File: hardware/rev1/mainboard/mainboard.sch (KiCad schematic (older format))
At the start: 59 parts, among them J1 CONN_05X2SHD, J2 Conn_01x10_Female, J3 Conn_01x10_Female, U1 LM1117-5.0, U2 LM1117-3.3, U3 SAMD51J, U4 OPA197, U5 W25Q32FVSS, U6 AD5685xRUZ, U7 SN74AHCT125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

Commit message: Switch 3v3 regulator to TPS796
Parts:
- removed U2: LM1117-3.3, Package_TO_SOT_SMD:SOT-223-3_TabPin2, symbol Regulator_Linear:LM1117-3.3
- added C21: 1uF, Capacitor_SMD:C_1206_3216Metric_Pad1.42x1.75mm_HandSolder, symbol Device:C
- added U2: TPS79633, Package_TO_SOT_SMD:SOT-223-6_TabPin3, symbol mainboard-rescue:TPS79633
- C7: value 22uF -> 4.7uF
- C8: value 22uF -> 0.1uF
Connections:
- wire segments 57 -> 61
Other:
- moved on the sheet: TP2
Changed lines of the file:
@@
 $EndComp
-$Comp
-L Regulator_Linear:LM1117-3.3 U2
-U 1 1 5D1ED054
-P 1400 2950
-F 0 "U2" H 1400 3192 50  0000 C CNN
-F 1 "LM1117-3.3" H 1400 3101 50  0000 C CNN
-F 2 "Package_TO_SOT_SMD:SOT-223-3_TabPin2" H 1400 2950 50  0001 C CNN
-F 3 "http://www.ti.com/lit/ds/symlink/lm1117.pdf" H 1400 2950 50  0001 C CNN
-	1    1400 2950
-	1    0    0    -1
-$EndComp
-$Comp
-L Device:C C7
-U 1 1 5D1EE7D9
-P 850 3100
-F 0 "C7" H 965 3146 50  0000 L CNN
-F 1 "22uF" H 965 3055 50  0000 L CNN
-F 2 "Capacitor_SMD:C_1206_3216Metric_Pad1.42x1.75mm_HandSolder" H 888 2950 50  0001 C CNN
-F 3 "~" H 850 3100 50  0001 C CNN
-	1    850  3100
-	1    0    0    -1
-$EndComp
-$Comp
-L Device:C C8
-U 1 1 5D341659
-P 1900 3100
-F 0 "C8" H 2015 3146 50  0000 L CNN
-F 1 "22uF" H 2015 3055 50  0000 L CNN
-F 2 "Capacitor_SMD:C_1206_3216Metric_Pad1.42x1.75mm_HandSolder" H 1938 2950 50  0001 C CNN
-F 3 "~" H 1900 3100 50  0001 C CNN
-	1    1900 3100
-	1    0    0    -1
-$EndComp
-Wire Wire Line
-	850  2950 1100 2950
-Wire Wire Line
-	1700 2950 1900 2950
-$Comp
-L power:GND #PWR0109
-U 1 1 5D1EFC36
-P 850 3250
-F 0 "#PWR0109" H 850 3000 50  0001 C CNN
-F 1 "GND" V 855 3122 50  0000 R CNN
-F 2 "" H 850 3250 50  0001 C CNN
-F 3 "" H 850 3250 50  0001 C CNN
-	1    850  3250
-	1    0    0    -1
-$EndComp
-$Comp
-L power:GND #PWR0110
-U 1 1 5D1F0162
-P 1400 3250
-F 0 "#PWR0110" H 1400 3000 50  0001 C CNN
-F 1 "GND" V 1405 3122 50  0000 R CNN
-F 2 "" H 1400 3250 50  0001 C CNN
-F 3 "" H 1400 3250 50  0001 C CNN
-	1    1400 3250
-	1    0    0    -1
-$EndComp
-$Comp
-L power:GND #PWR0111
-U 1 1 5D34165C
-P 1900 3250
-F 0 "#PWR0111" H 1900 3000 50  0001 C CNN
-F 1 "GND" V 1905 3122 50  0000 R CNN
-F 2 "" H 1900 3250 50  0001 C CNN
-F 3 "" H 1900 3250 50  0001 C CNN
-	1    1900 3250
-	1    0    0    -1
-$EndComp
-$Comp
-L power:+12V #PWR0112
-U 1 1 5D1F0712
-P 850 2950
-F 0 "#PWR0112" H 850 2800 50  0001 C CNN
-F 1 "+12V" H 865 3123 50  0000 C CNN
-F 2 "" H 850 2950 50  0001 C CNN
-F 3 "" H 850 2950 50  0001 C CNN
-	1    850  2950
-	1    0    0    -1
-$EndComp
-Connection ~ 850  2950
-$Comp
-L power:+3V3 #PWR0113
-U 1 1 5D1F0A40
-P 1900 2950
-F 0 "#PWR0113" H 1900 2800 50  0001 C CNN
-F 1 "+3V3" V 1900 3150 50  0000 C CNN
-F 2 "" H 1900 2950 50  0001 C CNN
-F 3 "" H 1900 2950 50  0001 C CNN
-	1    1900 2950
-	0    1    1    0
-$EndComp
-Connection ~ 1900 2950
 $Comp
 L Device:C C1
@@
 L Connector:TestPoint TP2
 U 1 1 5D263C38
-P 1900 2950
-F 0 "TP2" H 1950 3200 50  0000 L CNN
-F 1 "3.3v" H 1800 3200 50  0000 L CNN
-F 2 "TestPoint:TestPoint_THTPad_D1.5mm_Drill0.7mm" H 2100 2950 50  0001 C CNN
-F 3 "~" H 2100 2950 50  0001 C CNN
-	1    1900 2950
+P 2075 2850
+F 0 "TP2" H 2125 3100 50  0000 L CNN
+F 1 "3.3v" H 1975 3100 50  0000 L CNN
+F 2 "TestPoint:TestPoint_THTPad_D1.5mm_Drill0.7mm" H 2275 2850 50  0001 C CNN
+F 3 "~" H 2275 2850 50  0001 C CNN
+	1    2075 2850
 	1    0    0    -1
 $EndComp
@@
 	1    0    0    -1
 $EndComp
+$Comp
+L mainboard-rescue:TPS79633 U2
+U 1 1 5E1C19BB
+P 1475 2950
+F 0 "U2" H 1475 3292 50  0000 C CNN
+F 1 "TPS79633" H 1475 3201 50  0000 C CNN
+F 2 "Package_TO_SOT_SMD:SOT-223-6_TabPin3" H 1475 3275 50  0001 C CIN
+F 3 "http://www.ti.com/lit/ds/symlink/tps79333-ep.pdf" H 1475 3000 50  0001 C CNN
+	1    1475 2950
+	1    0    0    -1
+$EndComp
+Wire Wire Line
+	1175 3000 1000 3000
+Wire Wire Line
+	1000 3000 1000 2850
+Wire Wire Line
+	1175 2850 1000 2850
+$Comp
+L power:+5V #PWR0109
+U 1 1 5E1C6497
+P 800 2850
+F 0 "#PWR0109" H 800 2700 50  0001 C CNN
+F 1 "+5V" V 815 2978 50  0000 L CNN
+F 2 "" H 800 2850 50  0001 C CNN
+F 3 "" H 800 2850 50  0001 C CNN
+	1    800  2850
+	0    -1   -1   0
+$EndComp
+$Comp
+L Device:C C7
+U 1 1 5E1C8B98
+P 800 3000
+F 0 "C7" H 875 3075 50  0000 L CNN
+F 1 "4.7uF" H 850 2900 50  0000 L CNN
+F 2 "Capacitor_SMD:C_1206_3216Metric_Pad1.42x1.75mm_HandSolder" H 838 2850 50  0001 C CNN
+F 3 "~" H 800 3000 50  0001 C CNN
+	1    800  3000
+	1    0    0    -1
+$EndComp
+Wire Wire Line
+	775  2850 800  2850
+Connection ~ 800  2850
+Wire Wire Line
+	1000 2850 800  2850
+Connection ~ 1000 2850
+$Comp
+L power:GND #PWR0110
+U 1 1 5E1CC899
+P 1475 3250
+F 0 "#PWR0110" H 1475 3000 50  0001 C CNN
+F 1 "GND" V 1480 3122 50  0000 R CNN
+F 2 "" H 1475 3250 50  0001 C CNN
+F 3 "" H 1475 3250 50  0001 C CNN
+	1    1475 3250
+	1    0    0    -1
+$EndComp
+$Comp
+L power:+3V3 #PWR0111
+U 1 1 5E1CD045
+P 2075 2850
+F 0 "#PWR0111" H 2075 2700 50  0001 C CNN
+F 1 "+3V3" V 2075 3050 50  0000 C CNN
+F 2 "" H 2075 2850 50  0001 C CNN
+F 3 "" H 2075 2850 50  0001 C CNN
+	1    2075 2850
+	0    1    1    0
+$EndComp
+$Comp
+L Device:C C21
+U 1 1 5E1CD8BD
+P 2075 3000
+F 0 "C21" H 2190 3046 50  0000 L CNN
+F 1 "1uF" H 2190 2955 50  0000 L CNN
+F 2 "Capacitor_SMD:C_1206_3216Metric_Pad1.42x1.75mm_HandSolder" H 2113 2850 50  0001 C CNN
+F 3 "~" H 2075 3000 50  0001 C CNN
+	1    2075 3000
+	1    0    0    -1
+$EndComp
+Wire Wire Line
+	2075 2850 1775 2850
+Connection ~ 2075 2850
+$Comp
+L Device:C C8
+U 1 1 5E1D0271
+P 1775 3150
+F 0 "C8" H 1825 3250 50  0000 L CNN
+F 1 "0.1uF" H 1800 3050 50  0000 L CNN
+F 2 "Capacitor_SMD:C_1206_3216Metric_Pad1.42x1.75mm_HandSolder" H 1813 3000 50  0001 C CNN
+F 3 "~" H 1775 3150 50  0001 C CNN
+	1    1775 3150
+	1    0    0    -1
+$EndComp
+$Comp
+L power:GND #PWR0112
+U 1 1 5E1D081B
+P 1775 3300
+F 0 "#PWR0112" H 1775 3050 50  0001 C CNN
+F 1 "GND" V 1780 3172 50  0000 R CNN
+F 2 "" H 1775 3300 50  0001 C CNN
+F 3 "" H 1775 3300 50  0001 C CNN
+	1    1775 3300
+	1    0    0    -1
+$EndComp
+$Comp
+L power:GND #PWR0113
+U 1 1 5E1D0BB4
+P 2075 3150
+F 0 "#PWR0113" H 2075 2900 50  0001 C CNN
+F 1 "GND" V 2080 3022 50  0000 R CNN
+F 2 "" H 2075 3150 50  0001 C CNN
+F 3 "" H 2075 3150 50  0001 C CNN
+	1    2075 3150
+	1    0    0    -1
+$EndComp
+$Comp
+L power:GND #PWR0141
+U 1 1 5E1D0E81
+P 800 3150
+F 0 "#PWR0141" H 800 2900 50  0001 C CNN
+F 1 "GND" V 805 3022 50  0000 R CNN
+F 2 "" H 800 3150 50  0001 C CNN
+F 3 "" H 800 3150 50  0001 C CNN
+	1    800  3150
+	1    0    0    -1
+$EndComp

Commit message: Replace voltage reference buffer with OPA388
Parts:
- removed U4: OPA197, Package_TO_SOT_SMD:TSOT-23-5_HandSoldering, symbol precision-dac-cv-scaler:OPA197
- added U4: OPA388, Package_TO_SOT_SMD:TSOT-23-5_HandSoldering, symbol mainboard-rescue:OPA388
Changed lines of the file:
@@
-$EndComp
-$Comp
-L precision-dac-cv-scaler:OPA197 U4
-U 1 1 5E142769
-P 3300 1350
-F 0 "U4" H 3300 1600 50  0000 L CNN
-F 1 "OPA197" H 3300 1500 50  0000 L CNN
-F 2 "Package_TO_SOT_SMD:TSOT-23-5_HandSoldering" H 3200 1150 50  0001 L CNN
-F 3 "" H 3450 1500 50  0001 C CNN
-	1    3300 1350
-	1    0    0    -1
 $EndComp
 $Comp
@@
 	1    1800 900
 	0    1    1    0
-$EndComp
-$Comp
-L power:+12V #PWR0120
-U 1 1 5E17EE42
-P 3200 1050
-F 0 "#PWR0120" H 3200 900 50  0001 C CNN
-F 1 "+12V" V 3215 1178 50  0000 L CNN
-F 2 "" H 3200 1050 50  0001 C CNN
-F 3 "" H 3200 1050 50  0001 C CNN
-	1    3200 1050
-	1    0    0    -1
 $EndComp
 Text GLabel 3700 1350 2    50   Input ~ 0
@@
 	1    3750 1900
 	0    -1   -1   0
-$EndComp
-$Comp
-L power:+12V #PWR0148
-U 1 1 5E185FED
-P 3750 1600
-F 0 "#PWR0148" H 3750 1450 50  0001 C CNN
-F 1 "+12V" V 3765 1728 50  0000 L CNN
-F 2 "" H 3750 1600 50  0001 C CNN
-F 3 "" H 3750 1600 50  0001 C CNN
-	1    3750 1600
-	0    1    1    0
 $EndComp
 $Comp
@@
 	1    0    0    -1
 $EndComp
+$Comp
+L mainboard-rescue:OPA388 U4
+U 1 1 5E22D0F1
+P 3300 1350
+F 0 "U4" H 3300 1525 50  0000 L CNN
+F 1 "OPA388" H 3275 1200 50  0000 L CNN
+F 2 "Package_TO_SOT_SMD:TSOT-23-5_HandSoldering" H 3200 1150 50  0001 L CNN
+F 3 "http://www.ti.com/lit/ds/symlink/opa388.pdf" H 3450 1500 50  0001 C CNN
+	1    3300 1350
+	1    0    0    -1
+$EndComp
+$Comp
+L power:+3V3 #PWR0120
+U 1 1 5E24068B
+P 3200 1050
+F 0 "#PWR0120" H 3200 900 50  0001 C CNN
+F 1 "+3V3" V 3200 1250 50  0000 C CNN
+F 2 "" H 3200 1050 50  0001 C CNN
+F 3 "" H 3200 1050 50  0001 C CNN
+	1    3200 1050
+	1    0    0    -1
+$EndComp
+$Comp
+L power:+3V3 #PWR0148
+U 1 1 5E2413C8
+P 3750 1600
+F 0 "#PWR0148" H 3750 1450 50  0001 C CNN
+F 1 "+3V3" V 3750 1800 50  0000 C CNN
+F 2 "" H 3750 1600 50  0001 C CNN
+F 3 "" H 3750 1600 50  0001 C CNN
+	1    3750 1600
+	0    1    1    0
+$EndComp
 $EndSCHEMATC

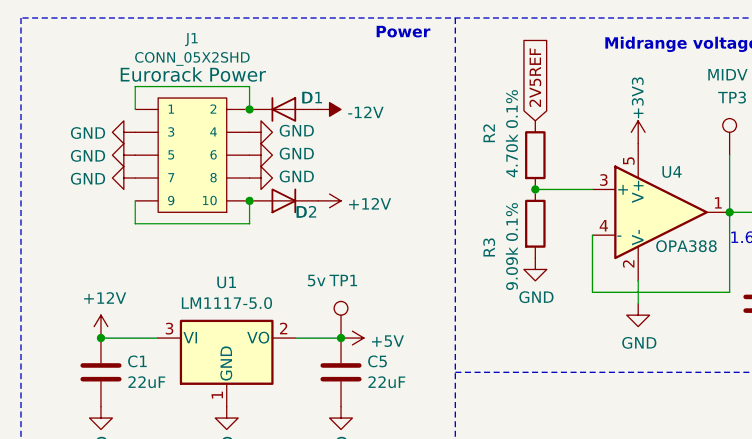
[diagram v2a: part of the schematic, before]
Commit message: Fix some component sizes
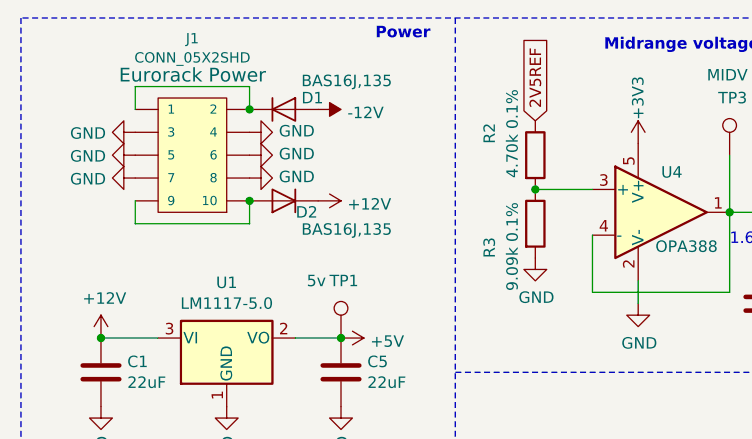
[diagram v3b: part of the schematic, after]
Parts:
- C2, C21, C8: footprint Capacitor_SMD:C_1206_3216Metric_Pad1.42x1.75mm_HandSolder -> Capacitor_SMD:C_0603_1608Metric_Pad1.05x0.95mm_HandSolder
- D1, D2: value D -> BAS16J,135; footprint Diode_SMD:D_0805_2012Metric_Pad1.15x1.40mm_HandSolder -> Diode_SMD:D_SOD-323F
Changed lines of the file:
@@
 P 1650 1300
 F 0 "D2" H 1550 1350 50  0000 C CNN
-F 1 "D" H 1575 1350 50  0000 C CNN
-F 2 "Diode_SMD:D_0805_2012Metric_Pad1.15x1.40mm_HandSolder" H 1650 1300 50  0001 C CNN
+F 1 "BAS16J,135" H 1375 1425 50  0000 C CNN
+F 2 "Diode_SMD:D_SOD-323F" H 1650 1300 50  0001 C CNN
 F 3 "~" H 1650 1300 50  0001 C CNN
 	1    1650 1300
@@
 F 0 "C2" H 1365 4346 50  0000 L CNN
 F 1 "1uF" H 1365 4255 50  0000 L CNN
-F 2 "Capacitor_SMD:C_1206_3216Metric_Pad1.42x1.75mm_HandSolder" H 1288 4150 50  0001 C CNN
+F 2 "Capacitor_SMD:C_0603_1608Metric_Pad1.05x0.95mm_HandSolder" H 1288 4150 50  0001 C CNN
 F 3 "~" H 1250 4300 50  0001 C CNN
 	1    1250 4300
@@
 P 1650 900
 F 0 "D1" H 1775 950 50  0000 C CNN
-F 1 "D" H 1750 950 50  0000 C CNN
-F 2 "Diode_SMD:D_0805_2012Metric_Pad1.15x1.40mm_HandSolder" H 1650 900 50  0001 C CNN
+F 1 "BAS16J,135" H 1925 1025 50  0000 C CNN
+F 2 "Diode_SMD:D_SOD-323F" H 1650 900 50  0001 C CNN
 F 3 "~" H 1650 900 50  0001 C CNN
 	1    1650 900
@@
 F 0 "C21" H 2190 3046 50  0000 L CNN
 F 1 "1uF" H 2190 2955 50  0000 L CNN
-F 2 "Capacitor_SMD:C_1206_3216Metric_Pad1.42x1.75mm_HandSolder" H 2113 2850 50  0001 C CNN
+F 2 "Capacitor_SMD:C_0603_1608Metric_Pad1.05x0.95mm_HandSolder" H 2113 2850 50  0001 C CNN
 F 3 "~" H 2075 3000 50  0001 C CNN
 	1    2075 3000
@@
 F 0 "C8" H 1825 3250 50  0000 L CNN
 F 1 "0.1uF" H 1800 3050 50  0000 L CNN
-F 2 "Capacitor_SMD:C_1206_3216Metric_Pad1.42x1.75mm_HandSolder" H 1813 3000 50  0001 C CNN
+F 2 "Capacitor_SMD:C_0603_1608Metric_Pad1.05x0.95mm_HandSolder" H 1813 3000 50  0001 C CNN
 F 3 "~" H 1775 3150 50  0001 C CNN
 	1    1775 3150

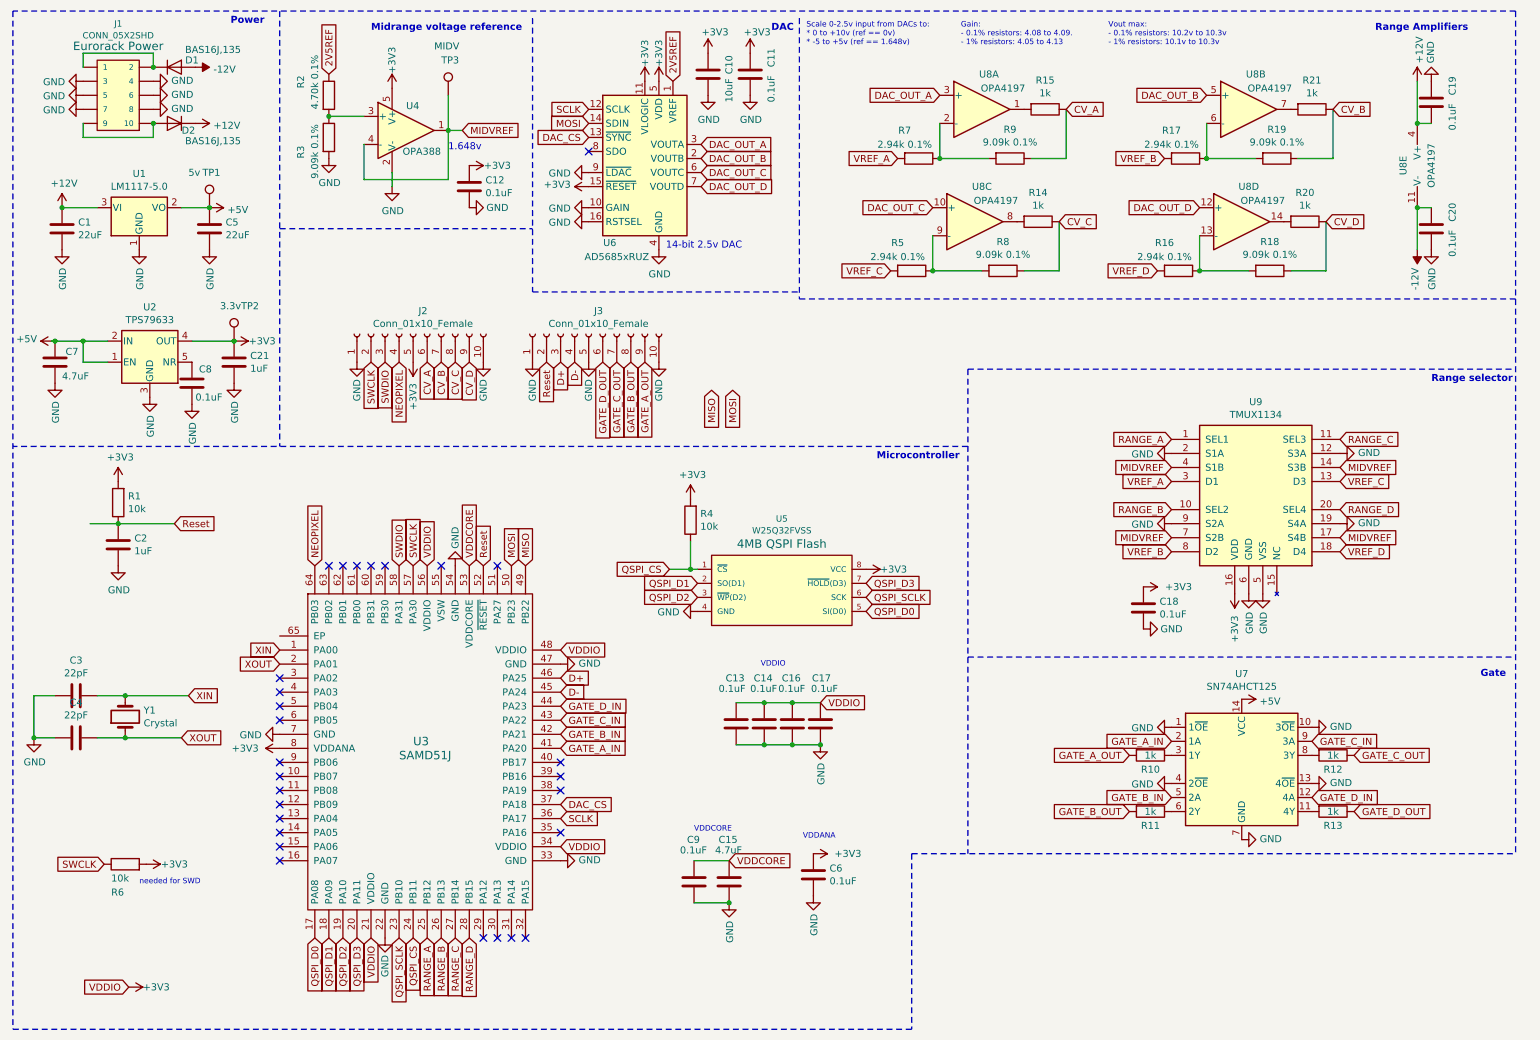
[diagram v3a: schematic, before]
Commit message: Move to the AD5686R, drop the TMUX
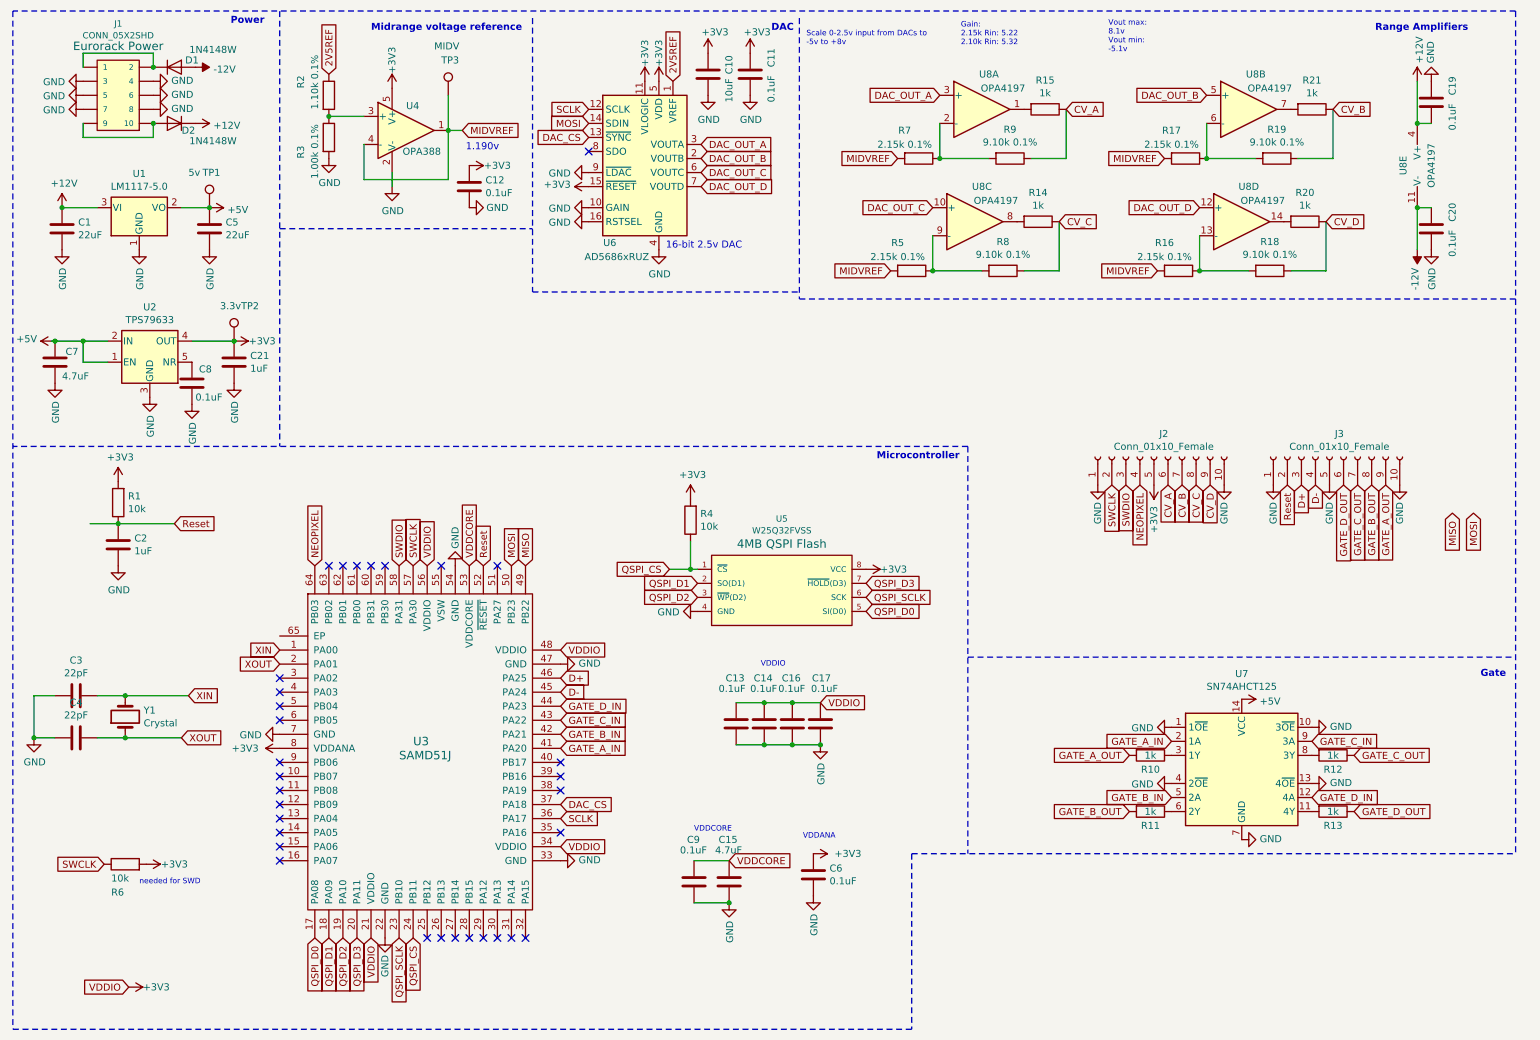
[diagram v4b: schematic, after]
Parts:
- removed C18: 0.1uF, Capacitor_SMD:C_0603_1608Metric_Pad1.05x0.95mm_HandSolder, symbol Device:C
- removed U9: TMUX1134, Package_SO:TSSOP-20_4.4x6.5mm_P0.65mm, symbol precision-dac-cv-scaler:TMUX1134
- D1, D2: value BAS16J,135 -> 1N4148W; footprint Diode_SMD:D_SOD-323F -> Diode_SMD:D_SOD-123
- R16, R17, R5, R7: value 2.94k 0.1% -> 2.15k 0.1%
- R18, R19, R8, R9: value 9.09k 0.1% -> 9.10k 0.1%
- R2: value 4.70k 0.1% -> 1.10k 0.1%
- R3: value 9.09k 0.1% -> 1.00k 0.1%
- U6: value AD5685xRUZ -> AD5686xRUZ
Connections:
- net labels removed: RANGE_A, RANGE_B, RANGE_C, RANGE_D, VREF_A, VREF_B, VREF_C, VREF_D
- no-connect marks 28 -> 32
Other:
- note added: "1.190v"
- note added: "16-bit 2.5v DAC"
- note added: "Gain:\n2.15k Rin: 5.22\n2.10k Rin: 5.32\n"
- note added: "Scale 0-2.5v input from DACs to\n-5v to +8v"
- note added: "Vout max:\n8.1v\nVout min:\n-5.1v"
- note removed: "1.648v"
- note removed: "14-bit 2.5v DAC"
- note removed: "Gain:\n- 0.1% resistors: 4.08 to 4.09.\n- 1% resistors: 4.05 to 4.13\n"
- note removed: "Range selector"
- note removed: "Scale 0-2.5v input from DACs to:\n* 0 to +10v (ref == 0v)\n* -5 to +5v (ref == 1.648v)"
- note removed: "Vout max:\n- 0.1% resistors: 10.2v to 10.3v\n- 1% resistors: 10.1v to 10.3v"
- moved on the sheet: J2, J3

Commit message: Update some cap sizes
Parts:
- C1, C5, C7: footprint Capacitor_SMD:C_1206_3216Metric_Pad1.42x1.75mm_HandSolder -> Capacitor_SMD:C_0805_2012Metric_Pad1.15x1.40mm_HandSolder
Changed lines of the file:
@@
 F 0 "C1" H 965 2096 50  0000 L CNN
 F 1 "22uF" H 965 2005 50  0000 L CNN
-F 2 "Capacitor_SMD:C_1206_3216Metric_Pad1.42x1.75mm_HandSolder" H 888 1900 50  0001 C CNN
+F 2 "Capacitor_SMD:C_0805_2012Metric_Pad1.15x1.40mm_HandSolder" H 888 1900 50  0001 C CNN
 F 3 "~" H 850 2050 50  0001 C CNN
 	1    850  2050
@@
 F 0 "C5" H 2015 2096 50  0000 L CNN
 F 1 "22uF" H 2015 2005 50  0000 L CNN
-F 2 "Capacitor_SMD:C_1206_3216Metric_Pad1.42x1.75mm_HandSolder" H 1938 1900 50  0001 C CNN
+F 2 "Capacitor_SMD:C_0805_2012Metric_Pad1.15x1.40mm_HandSolder" H 1938 1900 50  0001 C CNN
 F 3 "~" H 1900 2050 50  0001 C CNN
 	1    1900 2050
@@
 F 3 "" H 4600 1900 50  0001 C CNN
 	1    4600 1900
-	0    1    1    0
-$EndComp
-$Comp
-L power:GND #PWR0129
-U 1 1 5E13545E
-P 4600 2000
-F 0 "#PWR0129" H 4600 1750 50  0001 C CNN
-F 1 "GND" V 4605 1872 50  0000 R CNN
-F 2 "" H 4600 2000 50  0001 C CNN
-F 3 "" H 4600 2000 50  0001 C CNN
-	1    4600 2000
 	0    1    1    0
 $EndComp
@@
 F 0 "C7" H 875 3075 50  0000 L CNN
 F 1 "4.7uF" H 850 2900 50  0000 L CNN
-F 2 "Capacitor_SMD:C_1206_3216Metric_Pad1.42x1.75mm_HandSolder" H 838 2850 50  0001 C CNN
+F 2 "Capacitor_SMD:C_0805_2012Metric_Pad1.15x1.40mm_HandSolder" H 838 2850 50  0001 C CNN
 F 3 "~" H 800 3000 50  0001 C CNN
 	1    800  3000
@@
 NoConn ~ 3650 7100
 NoConn ~ 3750 7100
+$Comp
+L power:+3V3 #PWR?
+U 1 1 5E2E319B
+P 4600 2000
+F 0 "#PWR?" H 4600 1850 50  0001 C CNN
+F 1 "+3V3" V 4615 2128 50  0000 L CNN
+F 2 "" H 4600 2000 50  0001 C CNN
+F 3 "" H 4600 2000 50  0001 C CNN
+	1    4600 2000
+	0    -1   -1   0
+$EndComp
 $EndSCHEMATC

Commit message: Assign MPNs to all symbols
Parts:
- C1, C5: mpn (none) -> GRM21BR61E226ME44L
- C10: mpn (none) -> MF-CAP-1206-10uF
- C11, C12, C13, C14, C16, C17, C19, C20, C6, C8, C9: mpn (none) -> MF-CAP-0603-0.1uF
- C15: footprint Capacitor_SMD:C_1206_3216Metric_Pad1.42x1.75mm_HandSolder -> Capacitor_SMD:C_0805_2012Metric_Pad1.15x1.40mm_HandSolder; mpn (none) -> GRM21BZ71E475KE15L
- C2, C21: mpn (none) -> MF-CAP-0603-1uF
- C3, C4: mpn (none) -> MF-CAP-0603-22pF
- C7: mpn (none) -> GRM21BZ71E475KE15L
- D1, D2: mpn (none) -> 1N4148W
- R1, R4, R6: mpn (none) -> MF-RES-0805-10K
- R10, R11, R12, R13, R14, R15, R20, R21: mpn (none) -> MF-RES-0805-1K
- R18, R19, R8, R9: mpn (none) -> ERA8AEB9091V
- U1: mpn (none) -> LM1117IMPX-5.0/NOPB
- U2: mpn (none) -> TPS79633DCQR
- U3: mpn (none) -> ATSAMD51J20A-AUT
- U4: mpn (none) -> OPA388IDBVT
- U5: mpn (none) -> W25Q32JVSSIQ TR
- U6: mpn (none) -> AD5686RARUZ
- U7: mpn (none) -> SN74AHCT125QPWRQ1
- U8: mpn (none) -> OPA4197IPWR
- Y1: mpn (none) -> ABS06-32.768KHZ-1-T
